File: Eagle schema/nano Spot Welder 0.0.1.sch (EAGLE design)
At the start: 39 parts, among them Q1 BC548, Q3 BC138, T1 BTA 41 / 600V, U1 NANO, U2 DISPLAY-NOKIA-5110, U3 DS18B20, X3 ~230V, X4 Mikro trafó

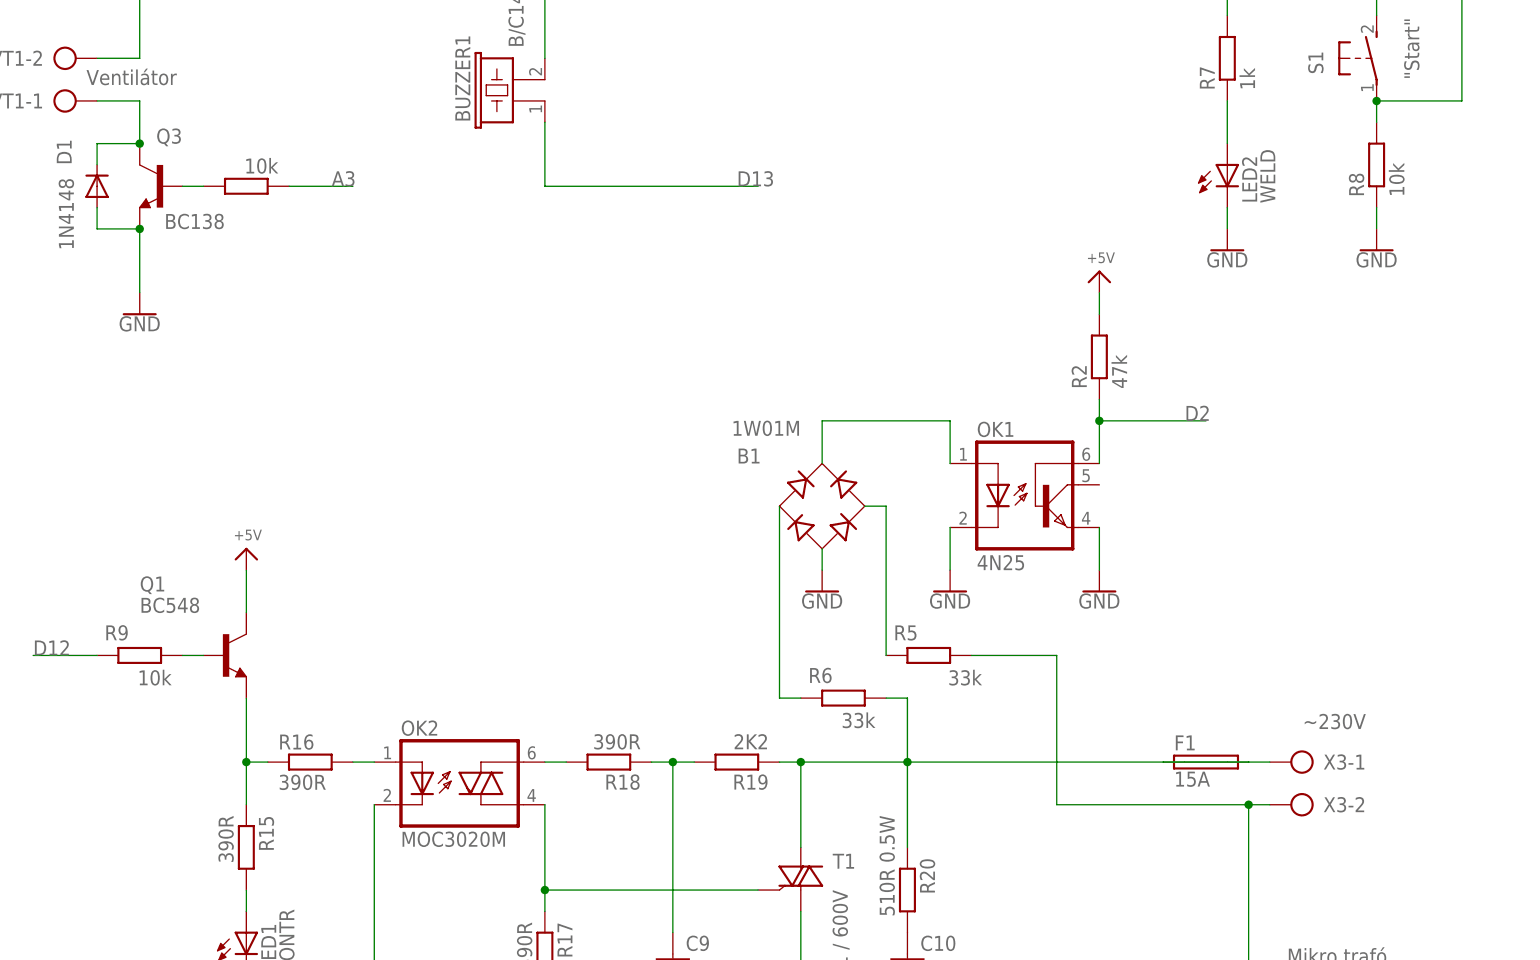
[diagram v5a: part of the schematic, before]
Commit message: - LM335 hőmérés - összerakott egységhez hangolás - environment.h
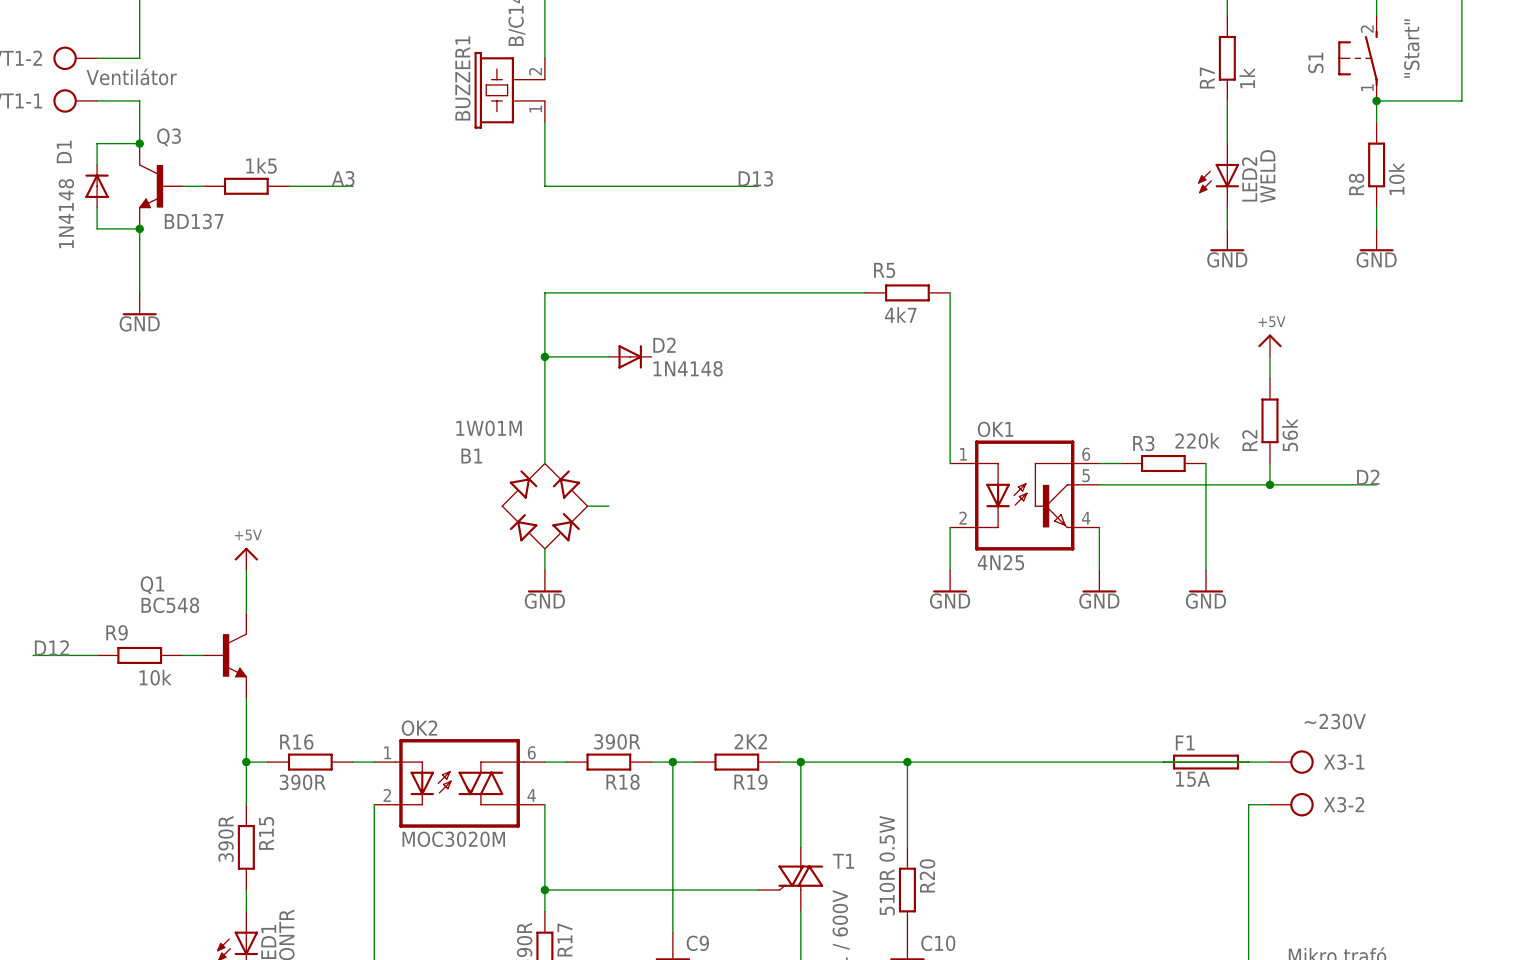
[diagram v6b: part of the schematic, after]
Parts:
- removed R6: 33k, resistor:R-EU_0204/7
- added D2: 1N4148, diode:1N4148DO35-10
- added R3: 220k, resistor:R-EU_0204/7
- Q3: value BC138 -> BD137
- R10: value 10k -> 1k5
- R2: value 47k -> 56k
- R5: value 33k -> 4k7
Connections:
- removed net N$24: B1.AC1, R6.2
- new net N$2: OK1.BAS, R3.1
- new net N$3: B1.+, D2.A, R5.2
- net D2: now also OK1.COL; no longer OK1.BAS
- net GND: now also R3.2
- net N$18: now also R5.1; no longer B1.+
- net N$21: no longer R5.2
- net N$25: no longer R6.1
- net N$28: no longer R5.1
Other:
- moved on the sheet: B1, R2, R5
